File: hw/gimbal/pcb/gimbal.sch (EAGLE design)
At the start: 80 parts, among them J1 JST-XH4SMT_RA, T12 TPPAD1-13, T3 TPPAD1-13, T8 TPPAD1-13, U1 STM32F4R_64PIN, U2 TPS62172PWSON8, U3 TPS55330PQFN16, U4 MC33926, U5 DRV8313, U6 DRV8313, U7 AS5048A

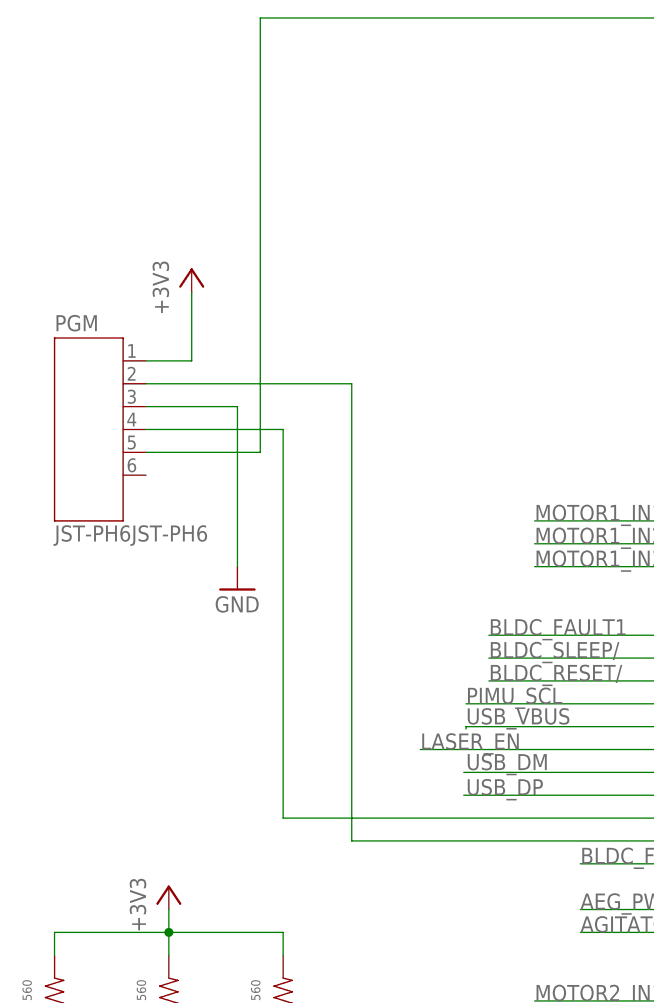
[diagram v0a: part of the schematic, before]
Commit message: gimbal: PCB: Fix the pin ordering on the programming connector.
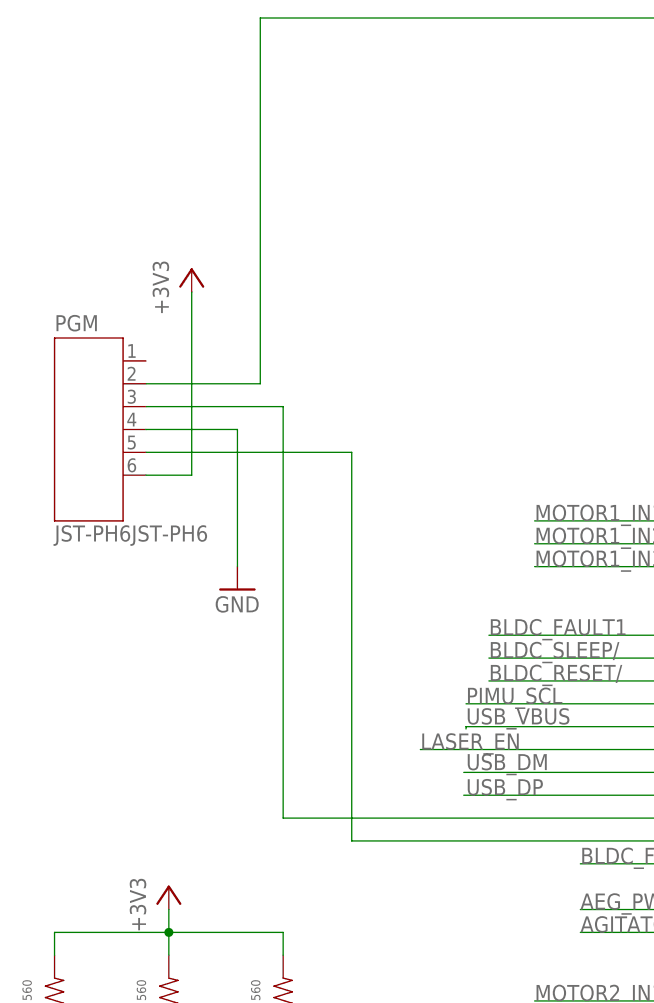
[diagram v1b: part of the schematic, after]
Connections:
- net +3V3: now also PGM.6; no longer PGM.1
- net GND: now also PGM.4; no longer PGM.3
- net N$24: now also PGM.2; no longer PGM.5
- net N$31: now also PGM.5; no longer PGM.2
- net N$32: now also PGM.3; no longer PGM.4
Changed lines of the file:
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@@
 </segment>
 <segment>
-<pinref part="PGM" gate="G$1" pin="3"/>
 <pinref part="GND16" gate="1" pin="GND"/>
-<wire x1="-30.48" y1="238.76" x2="-20.32" y2="238.76" width="0.1524" layer="91"/>
-<wire x1="-20.32" y1="238.76" x2="-20.32" y2="220.98" width="0.1524" layer="91"/>
+<pinref part="PGM" gate="G$1" pin="4"/>
+<wire x1="-20.32" y1="236.22" x2="-20.32" y2="220.98" width="0.1524" layer="91"/>
+<wire x1="-30.48" y1="236.22" x2="-20.32" y2="236.22" width="0.1524" layer="91"/>
 </segment>
 <segment>
@@
 </segment>
 <segment>
-<pinref part="PGM" gate="G$1" pin="1"/>
 <pinref part="+3V9" gate="G$1" pin="+3V3"/>
-<wire x1="-30.48" y1="243.84" x2="-25.4" y2="243.84" width="0.1524" layer="91"/>
-<wire x1="-25.4" y1="243.84" x2="-25.4" y2="251.46" width="0.1524" layer="91"/>
+<wire x1="-25.4" y1="251.46" x2="-25.4" y2="231.14" width="0.1524" layer="91"/>
+<pinref part="PGM" gate="G$1" pin="6"/>
+<wire x1="-25.4" y1="231.14" x2="-30.48" y2="231.14" width="0.1524" layer="91"/>
 </segment>
 <segment>
@@
 <junction x="101.6" y="264.16"/>
 <wire x1="101.6" y1="281.94" x2="-17.78" y2="281.94" width="0.1524" layer="91"/>
-<wire x1="-17.78" y1="281.94" x2="-17.78" y2="233.68" width="0.1524" layer="91"/>
-<pinref part="PGM" gate="G$1" pin="5"/>
-<wire x1="-17.78" y1="233.68" x2="-30.48" y2="233.68" width="0.1524" layer="91"/>
+<wire x1="-17.78" y1="281.94" x2="-17.78" y2="241.3" width="0.1524" layer="91"/>
 <pinref part="C6" gate="G$1" pin="P$1"/>
 <junction x="83.82" y="261.62"/>
+<pinref part="PGM" gate="G$1" pin="2"/>
+<wire x1="-17.78" y1="241.3" x2="-30.48" y2="241.3" width="0.1524" layer="91"/>
 </segment>
 </net>
 <net name="N$31" class="0">
 <segment>
-<pinref part="PGM" gate="G$1" pin="2"/>
-<wire x1="-30.48" y1="241.3" x2="-7.62" y2="241.3" width="0.1524" layer="91"/>
-<wire x1="-7.62" y1="241.3" x2="-7.62" y2="190.5" width="0.1524" layer="91"/>
 <pinref part="U1" gate="G$1" pin="PA14/SWCLK"/>
+<wire x1="-7.62" y1="233.68" x2="-7.62" y2="190.5" width="0.1524" layer="91"/>
 <wire x1="-7.62" y1="190.5" x2="48.006" y2="190.5" width="0.1524" layer="91"/>
+<pinref part="PGM" gate="G$1" pin="5"/>
+<wire x1="-30.48" y1="233.68" x2="-7.62" y2="233.68" width="0.1524" layer="91"/>
 </segment>
 </net>
 <net name="N$32" class="0">
 <segment>
-<wire x1="-15.24" y1="193.04" x2="-15.24" y2="236.22" width="0.1524" layer="91"/>
-<pinref part="PGM" gate="G$1" pin="4"/>
-<wire x1="-15.24" y1="236.22" x2="-30.48" y2="236.22" width="0.1524" layer="91"/>
+<wire x1="-15.24" y1="193.04" x2="-15.24" y2="238.76" width="0.1524" layer="91"/>
 <pinref part="U1" gate="G$1" pin="PA13/SWDIO"/>
 <wire x1="-15.24" y1="193.04" x2="48.006" y2="193.04" width="0.1524" layer="91"/>
-</segment>
-</net>
+<pinref part="PGM" gate="G$1" pin="3"/>
+<wire x1="-15.24" y1="238.76" x2="-30.48" y2="238.76" width="0.1524" layer="91"/>
+</segment>
+</net>

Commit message: gimbal: Start work on updating gimbal board to support mounting a joule shield on top of it.
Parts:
- removed C15: 100uF, mfpassives:CAPACITOR_P_6.3MM
- removed R19, R20: 1.69k, mfpassives:RESISTOR_0603
- removed SIMU: JST-ZH4, gimbal:JST-ZH4
- removed USB: MICRO-USB, gimbal:MICRO-USB
- removed USBI: (no value), gimbal:JST-PH4RA
- removed USBO: (no value), gimbal:JST-PH4SMT_VERT
- added C28, C29: 47uF, rcl:C-USC1206
- added J3: JST-XH4SMT_RA, gimbal:JST-XH4SMT_RA
- added J4: MF-CON-MICROUSB-RIGHT, mf_connectors:USB_MICRO_RIGHT
- added U$52, U$53, U$54, U$55: M2.5MOUNT, joule_shield:M2.5MOUNT
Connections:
- removed net N$12: USBI.1, USBO.1
- removed net N$13: USBI.2, USBO.2
- removed net N$14: USBI.3, USBO.3
- removed net N$15: USBI.4, USBO.4
- net +12V: now also C28.1, C29.1; no longer C15.P$1
- net +3V3: no longer R19.P$2, R20.P$2, SIMU.1
- net +8V: now also J3.4
- net GND: now also C28.2, C29.2, J3.1, J4.GND, J4.SLD; no longer C15.P$2, SIMU.4, USBG$1.5
- net SIMU_SCL: no longer R20.P$1, SIMU.3
- net SIMU_SDA: no longer R19.P$1, SIMU.2
- net SLAVE_RX: now also J3.3
- net SLAVE_TX: now also J3.2
- net USB_DM: now also J4.D-; no longer USBG$1.2
- net USB_DP: now also J4.D+; no longer USBG$1.3
- net USB_VBUS: now also J4.5V; no longer USBG$1.1

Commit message: WIP on 18V rs485 version of gimbal board
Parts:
- removed C28, C29: 47uF, rcl:C-USC1206
- removed C7: 4.7uF, mfpassives:CAPACITOR_NP_0603
- removed D4: DIODEB520C, gimbal:DIODEB520C
- removed J4: MF-CON-MICROUSB-RIGHT, mf_connectors:USB_MICRO_RIGHT
- removed L1: 2.2uH, gimbal:INDL1212
- removed PGM: JST-PH6JST-PH6, gimbal:JST-PH6JST-PH6
- removed R10, R8: 10k, mfpassives:RESISTOR_0603
- removed R11: 78.7k, mfpassives:RESISTOR_0603
- removed R12: 1.87k, mfpassives:RESISTOR_0603
- removed R14: 220, mfpassives:RESISTOR_0603
- removed R9: 88.7k, mfpassives:RESISTOR_0603
- removed T12, T3, T8, TG: TPPAD1-13, testpad:TPPAD1-13
- removed U$52, U$53, U$54, U$55: M2.5MOUNT, joule_shield:M2.5MOUNT
- added C15: 0.1uF 50V, mfpassives:CAPACITOR_NP_0402
- added SWD: JST-ZH6SMT_VERT, controller:JST-ZH6SMT_VERT
- ARM: AMFPN JS102011SAQN -> (none); DPN 401-1999-1-ND -> (none); MPN (none) -> JS102011SAQN; POPULATE (none) -> 1
- C1: value 4.7uF -> 10uF 35V; device mfpassives:CAPACITOR_NP_0603 -> mfpassives:CAPACITOR_NP_1206; AMFPN CC0603KRX5R6BB475 -> (none); DPN 311-1455-1-ND -> (none); MF (none) -> TDK; MPN (none) -> CGA5L1X7R1V106K160AC
- C10: value 10uF -> 0.1uF 50V; device mfpassives:CAPACITOR_NP_1206 -> mfpassives:CAPACITOR_NP_0402; AMFPN MF-CAP-1206-10uF -> (none); MF (none) -> Walsin; MPN (none) -> 0402B104K500CT
- C11, C17, C18, C19: value 22uF 16V -> 10uF 35V; device mfpassives:CAPACITOR_NP_1210 -> mfpassives:CAPACITOR_NP_1206; AMFPN C3225X7R1C226M250AC -> (none); DPN 445-3955-1-ND -> (none); MF (none) -> TDK; MPN (none) -> CGA5L1X7R1V106K160AC
- C12, C16: value 10uF -> 10uF 35V; AMFPN MF-CAP-1206-10uF -> (none); MF (none) -> TDK; MPN (none) -> CGA5L1X7R1V106K160AC
- C13: value 0.047uF -> 10uF 35V; device mfpassives:CAPACITOR_NP_0603 -> mfpassives:CAPACITOR_NP_1206; AMFPN GRM188R71E473KA01D -> (none); DPN 490-1522-1-ND -> (none); MF (none) -> TDK; MPN (none) -> CGA5L1X7R1V106K160AC
- C14: value 0.1uF -> 10uF 35V; device mfpassives:CAPACITOR_NP_0603 -> mfpassives:CAPACITOR_NP_1206; AMFPN MF-CAP-0603-0.1uF -> (none); MF (none) -> TDK; MPN (none) -> CGA5L1X7R1V106K160AC
- C2, C20, C21, C22, C24, C26, C27, C3, C4, C5, C6: value 0.1uF -> 0.1uF 50V; device mfpassives:CAPACITOR_NP_0603 -> mfpassives:CAPACITOR_NP_0402; AMFPN MF-CAP-0603-0.1uF -> (none); MF (none) -> Walsin; MPN (none) -> 0402B104K500CT
- C23, C25: AMFPN MF-CAP-0603-0.01uF -> (none); HOUSEPART (none) -> YES; MPN (none) -> MF-CAP-0603-0.01uF
- C8, C9: AMFPN MF-CAP-0603-10pF -> (none); HOUSEPART (none) -> YES; MPN (none) -> MF-CAP-0603-10pF
- D1: device mfleds:LED_SINGLE_0603 -> mfleds:LED_SINGLE-0603-RED; AMFPN MF-LED-0603-GREEN -> (none)
- D2, D3: device mfleds:LED_SINGLE_0603 -> mfleds:LED_SINGLE-0603-RED; AMFPN MF-LED-0603-RED -> (none)
- J1, J3: AMFPN S4B-XH-SM4-TB(LF)(SN) -> (none); DPN 455-2262-1-ND -> (none); MF (none) -> JST; MPN (none) -> S4B-XH-SM4-TB(LF)(SN); POPULATE (none) -> 1
- J2, M1, M2, MOUNT1, MOUNT2: POPULATE (none) -> 0
- L2: value 2.2uH -> 10uH; device gimbal:INDASPI-6045S -> mfpassives:INDUCTOR_1210; AMFPN ASPI-6045S-2R2N-T -> (none); DPN ASPI-6045S-2R2N-TCT-ND -> (none); HOUSEPART (none) -> 1; MPN (none) -> MF-IND-1210-10uH; POPULATE (none) -> 1
- PABS, PI: AMFPN B4B-ZR-SM4-TF(LF)(SN) -> (none); DPN 455-1683-1-ND -> (none); MF (none) -> JST; MPN (none) -> B4B-ZR-SM4-TF(LF)(SN); POPULATE (none) -> 1
- Q1: AMFPN ABM3B-8.000MHZ-10-1-U-T -> (none); DPN 535-9721-1-ND -> (none); MPN (none) -> ABM3B-8.000MHZ-10-1-U-T; POPULATE (none) -> 1
- R1: value 10 -> 560; AMFPN MF-RES-0603-10 -> (none); HOUSEPART (none) -> YES; MPN (none) -> MF-RES-0603-560
- R13, R5: value 100k -> 18k; AMFPN ERJ-3EKF1003V -> (none); DPN P100KHCT-ND -> (none); HOUSEPART (none) -> YES; MPN (none) -> MF-RES-0603-18K
- R15, R16, R17, R18: AMFPN MF-RES-0603-1.69K -> (none); HOUSEPART (none) -> YES; MPN (none) -> MF-RES-0603-1.69K
- R2, R3, R4: AMFPN MF-RES-0603-560 -> (none); HOUSEPART (none) -> YES; MPN (none) -> MF-RES-0603-560
- R6: value 10k -> 1.69k; AMFPN ERJ-3EKF1002V -> (none); DPN P10.0KHCT-ND -> (none); HOUSEPART (none) -> YES; MPN (none) -> MF-RES-0603-1.69K
- R7: value 100k -> 560; AMFPN ERJ-3EKF1003V -> (none); DPN P100KHCT-ND -> (none); HOUSEPART (none) -> YES; MPN (none) -> MF-RES-0603-560
- U1: AMFPN STM32F411RET6 -> (none); DPN 497-14909-ND -> (none); MF (none) -> ST; MPN (none) -> STM32F411RET6; POPULATE (none) -> 1
- U2: value TPS62172PWSON8 -> MAX13431E; device gimbal:TPS62172PWSON8 -> controller:MAX13431E; AMFPN TPS62172DSGT -> (none); DPN 296-29879-1-ND -> (none); MF (none) -> Maxim; MPN (none) -> MAX13431EETB+T; POPULATE (none) -> 1
- U3: value TPS55330PQFN16 -> TPS62177WSON10; device gimbal:TPS55330PQFN16 -> imu_junction:TPS62177WSON10; AMFPN TPS55330RTET -> (none); DPN 296-36219-1-ND -> (none); MF (none) -> TI; MPN (none) -> TPS62177DQCR; POPULATE (none) -> 1
- U4: AMFPN MC33926PNBR2 -> (none); DPN MC33926PNBR2CT-ND -> (none); MF (none) -> Freescale; MPN (none) -> MC33926PNBR2; POPULATE (none) -> 1
- U5, U6: AMFPN DRV8313PWP -> (none); DPN 296-35540-5-ND -> (none); MF (none) -> TI; MPN (none) -> DRV8313PWP; POPULATE (none) -> 1
- U7: AMFPN AS5048A-HTSP-500 -> (none); DPN AS5048A-HTSP-500CT-ND -> (none); MF (none) -> austriamicrosystems; MPN (none) -> AS5048A-HTSP-500; POPULATE (none) -> 1
- U8: AMFPN MF-DSC-SOT233-BSS138 -> (none); HOUSEPART (none) -> YES; MPN (none) -> MF-DSC-SOT233-BSS138; POPULATE (none) -> 1
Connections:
- removed net +12V: C16.P$1, C22.P$1, C24.P$1, C28.1, C29.1, D4.1, R7.P$2, R9.P$2, T12.TP, U5.VM1, U5.VM2, U6.VM1, U6.VM2
- removed net BOOST_EN: U1.PC3/SPI2_MOSI, U3.EN
- removed net N$16: L1.P$1, U2.SW
- removed net N$17: D4.2, L2.P$2, U3.SW1, U3.SW2, U3.SW3
- removed net N$18: R11.P$2, U3.FREQ
- removed net N$19: C14.P$1, R12.P$1
- removed net N$20: R12.P$2, U3.COMP
- removed net N$21: C13.P$1, U3.SS
- removed net N$22: R10.P$2, R9.P$1, U3.FB
- removed net N$38: R7.P$1, R8.P$2, U1.PC2/SPI2_MISO
- removed net SIMU_SCL: U1.PB10/TIM2_3/I2C2_SCL/SPI2_SCK
- removed net SIMU_SDA: U1.PB9/TIM4_4/TIM11_1/I2C1_SDA/I2C2_SDA
- removed net USB_DM: J4.D-, U1.PA11/TIM1_4/SPI4_MISO/UART6_TX/USB_DM
- removed net USB_DP: J4.D+, U1.PA12/SPI5_MISO/UART6_RX/USB_DP
- removed net USB_VBUS: J4.5V, U1.PA9/TIM1_2/UART1_TX/USB_VBUS
- new net D1_N: J1.3, J3.3, U2.B
- new net D1_P: J1.2, J3.2, U2.A
- new net DIR3: U2.DE, U2.RE/
- new net N$4: L2.P$1, U3.SW
- net +3V3: now also C10.P$1, C13.P$1, C14.P$1, C15.P$1, L2.P$2, SWD.6, U2.VCC, U2.VL, U3.SLEEP, U3.VOS; no longer C1.P$1, C11.P$1, L1.P$2, PGM.6, T3.TP, U2.VOS
- net +8V: now also C11.P$1, C16.P$1, C22.P$1, C24.P$1, U3.EN, U5.VM1, U5.VM2, U6.VM1, U6.VM2; no longer C10.P$1, L2.P$1, T8.TP, U2.EN, U2.VIN
- net GND: now also C15.P$2, R7.P$1, SWD.4, U2.GND, U3.FB, U3.NC, U3.PGND; no longer C28.2, C29.2, C7.P$2, J4.GND, J4.SLD, PGM.4, R10.P$1, R11.P$1, R14.P$1, R8.P$1, TG.TP, U2.AGND, U2.FB, U2.PGND, U3.PGND1, U3.PGND2, U3.PGND3
- net MOTOR_FB: now also R7.P$2; no longer R14.P$2
- net N$23: now also C1.P$1; no longer C7.P$1
- net N$24: now also SWD.2; no longer PGM.2
- net N$31: now also SWD.5; no longer PGM.5
- net N$32: now also SWD.3; no longer PGM.3
- net SLAVE_RX: now also U2.RO; no longer J1.3, J3.3
- net SLAVE_TX: now also U2.DI; no longer J1.2, J3.2
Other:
- moved on the sheet: J3, R1, R13, R15, R16, R17, R18, R2, R3, R4, R5, R6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

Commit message: More work on gimbal v4
Power and ground now largely routed
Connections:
- net +8V renamed +18V
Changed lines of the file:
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@@
 <part name="+3V6" library="supply1" deviceset="+3V3" device=""/>
 <part name="GND11" library="supply1" deviceset="GND" device=""/>
-<part name="SUPPLY3" library="supply2" deviceset="+8V" device=""/>
+<part name="SUPPLY3" library="supply2" deviceset="+18V" device=""/>
 <part name="GND12" library="supply1" deviceset="GND" device=""/>
 <part name="GND13" library="supply1" deviceset="GND" device=""/>
@@
 </part>
 <part name="GND17" library="supply1" deviceset="GND" device=""/>
-<part name="SUPPLY4" library="supply2" deviceset="+8V" device=""/>
+<part name="SUPPLY4" library="supply2" deviceset="+18V" device=""/>
 <part name="GND18" library="supply1" deviceset="GND" device=""/>
 <part name="ARM" library="gimbal" deviceset="SLIDE_SWITCH" device="JS_SUB_SWITCH">
@@
 <attribute name="MPN" value="CGA5L1X7R1V106K160AC"/>
 </part>
-<part name="SUPPLY5" library="supply2" deviceset="+8V" device=""/>
+<part name="SUPPLY5" library="supply2" deviceset="+18V" device=""/>
 <part name="R17" library="mfpassives" deviceset="RESISTOR" device="_0603" value="1.69k">
 <attribute name="HOUSEPART" value="YES"/>
@@
 <attribute name="POPULATE" value="1"/>
 </part>
-<part name="SUPPLY2" library="supply2" deviceset="+8V" device=""/>
-<part name="SUPPLY6" library="supply2" deviceset="+8V" device=""/>
+<part name="SUPPLY2" library="supply2" deviceset="+18V" device=""/>
+<part name="SUPPLY6" library="supply2" deviceset="+18V" device=""/>
 <part name="U3" library="imu_junction" deviceset="TPS62177" device="WSON10">
 <attribute name="MF" value="TI"/>
@@
 <attribute name="MPN" value="0402B104K500CT"/>
 </part>
-<part name="SUPPLY7" library="supply2" deviceset="+8V" device=""/>
+<part name="SUPPLY7" library="supply2" deviceset="+18V" device=""/>
 <part name="GND7" library="supply1" deviceset="GND" device=""/>
 <part name="U2" library="controller" deviceset="MAX13431E" device="">
@@
 <instance part="+3V6" gate="G$1" x="25.4" y="-292.1"/>
 <instance part="GND11" gate="1" x="101.6" y="-403.86"/>
-<instance part="SUPPLY3" gate="+8V" x="111.76" y="-375.92"/>
+<instance part="SUPPLY3" gate="+18V" x="111.76" y="-375.92"/>
 <instance part="GND12" gate="1" x="63.5" y="-210.82"/>
 <instance part="GND13" gate="1" x="226.06" y="-210.82"/>
@@
 </instance>
 <instance part="GND17" gate="1" x="203.2" y="142.24"/>
-<instance part="SUPPLY4" gate="+8V" x="226.06" y="236.22"/>
+<instance part="SUPPLY4" gate="+18V" x="226.06" y="236.22"/>
 <instance part="GND18" gate="1" x="226.06" y="180.34"/>
 <instance part="ARM" gate="G$1" x="104.14" y="-101.6">
@@
 <attribute name="MF" x="60.96" y="-48.26" size="1.778" layer="96" display="off"/>
 </instance>
-<instance part="SUPPLY5" gate="+8V" x="43.18" y="-17.78"/>
+<instance part="SUPPLY5" gate="+18V" x="43.18" y="-17.78"/>
 <instance part="R17" gate="G$1" x="91.44" y="-314.96" rot="R180"/>
 <instance part="R18" gate="G$1" x="96.52" y="-314.96" rot="R180"/>
@@
 <attribute name="POPULATE" x="48.26" y="-388.62" size="1.778" layer="96" display="off"/>
 </instance>
-<instance part="SUPPLY2" gate="+8V" x="7.62" y="-121.92"/>
-<instance part="SUPPLY6" gate="+8V" x="167.64" y="-127"/>
+<instance part="SUPPLY2" gate="+18V" x="7.62" y="-121.92"/>
+<instance part="SUPPLY6" gate="+18V" x="167.64" y="-127"/>
 <instance part="U3" gate="G$1" x="170.18" y="58.42">
 <attribute name="MPN" x="170.18" y="58.42" size="1.778" layer="96" display="off"/>
@@
 <attribute name="MF" x="226.06" y="53.34" size="1.778" layer="96" display="off"/>
 </instance>
-<instance part="SUPPLY7" gate="+8V" x="132.08" y="76.2"/>
+<instance part="SUPPLY7" gate="+18V" x="132.08" y="76.2"/>
 <instance part="GND7" gate="1" x="111.76" y="-469.9"/>
 <instance part="U2" gate="G$1" x="78.74" y="-444.5">
@@
 </segment>
 </net>
-<net name="+8V" class="0">
+<net name="+18V" class="0">
 <segment>
 <pinref part="J1" gate="G$1" pin="4"/>
-<pinref part="SUPPLY3" gate="+8V" pin="+8V"/>
+<pinref part="SUPPLY3" gate="+18V" pin="+18V"/>
 <wire x1="88.9" y1="-391.16" x2="111.76" y2="-391.16" width="0.1524" layer="91"/>
 <wire x1="111.76" y1="-391.16" x2="111.76" y2="-378.46" width="0.1524" layer="91"/>
@@
 </segment>
 <segment>
-<pinref part="SUPPLY4" gate="+8V" pin="+8V"/>
+<pinref part="SUPPLY4" gate="+18V" pin="+18V"/>
 <wire x1="226.06" y1="233.68" x2="226.06" y2="231.14" width="0.1524" layer="91"/>
 <pinref part="R5" gate="G$1" pin="P$2"/>
@@
 <pinref part="C18" gate="G$1" pin="P$1"/>
 <pinref part="C19" gate="G$1" pin="P$1"/>
-<pinref part="SUPPLY5" gate="+8V" pin="+8V"/>
+<pinref part="SUPPLY5" gate="+18V" pin="+18V"/>
 <junction x="43.18" y="-20.32"/>
 </segment>
@@
 <wire x1="12.7" y1="-137.16" x2="17.78" y2="-137.16" width="0.1524" layer="91"/>
 <pinref part="C22" gate="G$1" pin="P$1"/>
-<pinref part="SUPPLY2" gate="+8V" pin="+8V"/>
+<pinref part="SUPPLY2" gate="+18V" pin="+18V"/>
 <pinref part="C11" gate="G$1" pin="P$1"/>
 <wire x1="7.62" y1="-124.46" x2="-27.94" y2="-124.46" width="0.1524" layer="91"/>
@@
 <wire x1="170.18" y1="-139.7" x2="177.8" y2="-139.7" width="0.1524" layer="91"/>
 <pinref part="C24" gate="G$1" pin="P$1"/>
-<pinref part="SUPPLY6" gate="+8V" pin="+8V"/>
+<pinref part="SUPPLY6" gate="+18V" pin="+18V"/>
 <pinref part="C16" gate="G$1" pin="P$1"/>
 <wire x1="132.08" y1="-137.16" x2="132.08" y2="-132.08" width="0.1524" layer="91"/>
@@
 <wire x1="132.08" y1="68.58" x2="132.08" y2="53.34" width="0.1524" layer="91"/>
 <junction x="132.08" y="68.58"/>
-<pinref part="SUPPLY7" gate="+8V" pin="+8V"/>
-</segment>
-</net>
+<pinref part="SUPPLY7" gate="+18V" pin="+18V"/>
+</segment>
+</net>

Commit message: More work on gimbal r4
I think everything is ready now
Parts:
- removed J3: JST-XH4SMT_RA, gimbal:JST-XH4SMT_RA
- added JW: (no value), pinhead:PINHD-2X4
- J2: value (none) -> JST-XH4SMT_RA; device pinhead:PINHD-2X4 -> gimbal:JST-XH4SMT_RA; MF (none) -> JST; MPN (none) -> S4B-XH-SM4-TB(LF)(SN); POPULATE 0 -> 1
- U7: MF austriamicrosystems -> AMS; MPN AS5048A-HTSP-500 -> AS5047P-ATSM
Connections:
- removed net DIR3: U2.DE, U2.RE/
- new net SLAVE_DIR: U1.PC8/TIM3_3, U2.DE, U2.RE/
- net +18V: now also J2.4; no longer J3.4
- net +3V3: now also JW.5; no longer J2.5
- net D1_N: now also J2.3; no longer J3.3
- net D1_P: now also J2.2; no longer J3.2
- net GND: now also J2.1, JW.2, JW.4; no longer J2.2, J2.4, J3.1
- net N$1: now also JW.6; no longer J2.6
- net N$2: now also JW.3; no longer J2.3
- net N$3: now also JW.1; no longer J2.1
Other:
- moved on the sheet: C6, R1

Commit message: gimbal: Replace 10uF cap with one that exists
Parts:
- C1, C11, C12, C13, C14, C16, C17, C18, C19: MPN CGA5L1X7R1V106K160AC -> CGA5L1X7R1V106M160AE
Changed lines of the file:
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@@
 <part name="C17" library="mfpassives" deviceset="CAPACITOR_NP" device="_1206" value="10uF 35V">
 <attribute name="MF" value="TDK"/>
-<attribute name="MPN" value="CGA5L1X7R1V106K160AC"/>
+<attribute name="MPN" value="CGA5L1X7R1V106M160AE"/>
 </part>
 <part name="C18" library="mfpassives" deviceset="CAPACITOR_NP" device="_1206" value="10uF 35V">
 <attribute name="MF" value="TDK"/>
-<attribute name="MPN" value="CGA5L1X7R1V106K160AC"/>
+<attribute name="MPN" value="CGA5L1X7R1V106M160AE"/>
 </part>
 <part name="C19" library="mfpassives" deviceset="CAPACITOR_NP" device="_1206" value="10uF 35V">
 <attribute name="MF" value="TDK"/>
-<attribute name="MPN" value="CGA5L1X7R1V106K160AC"/>
+<attribute name="MPN" value="CGA5L1X7R1V106M160AE"/>
 </part>
 <part name="SUPPLY5" library="supply2" deviceset="+18V" device=""/>
@@
 <part name="C13" library="mfpassives" deviceset="CAPACITOR_NP" device="_1206" value="10uF 35V">
 <attribute name="MF" value="TDK"/>
-<attribute name="MPN" value="CGA5L1X7R1V106K160AC"/>
+<attribute name="MPN" value="CGA5L1X7R1V106M160AE"/>
 </part>
 <part name="C14" library="mfpassives" deviceset="CAPACITOR_NP" device="_1206" value="10uF 35V">
 <attribute name="MF" value="TDK"/>
-<attribute name="MPN" value="CGA5L1X7R1V106K160AC"/>
+<attribute name="MPN" value="CGA5L1X7R1V106M160AE"/>
 </part>
 <part name="C12" library="mfpassives" deviceset="CAPACITOR_NP" device="_1206" value="10uF 35V">
 <attribute name="MF" value="TDK"/>
-<attribute name="MPN" value="CGA5L1X7R1V106K160AC"/>
+<attribute name="MPN" value="CGA5L1X7R1V106M160AE"/>
 </part>
 <part name="C15" library="mfpassives" deviceset="CAPACITOR_NP" device="_0402" value="0.1uF 50V">
@@
 <part name="C11" library="mfpassives" deviceset="CAPACITOR_NP" device="_1206" value="10uF 35V">
 <attribute name="MF" value="TDK"/>
-<attribute name="MPN" value="CGA5L1X7R1V106K160AC"/>
+<attribute name="MPN" value="CGA5L1X7R1V106M160AE"/>
 </part>
 <part name="C16" library="mfpassives" deviceset="CAPACITOR_NP" device="_1206" value="10uF 35V">
 <attribute name="MF" value="TDK"/>
-<attribute name="MPN" value="CGA5L1X7R1V106K160AC"/>
+<attribute name="MPN" value="CGA5L1X7R1V106M160AE"/>
 </part>
 <part name="GND3" library="supply1" deviceset="GND" device=""/>
@@
 <part name="C1" library="mfpassives" deviceset="CAPACITOR_NP" device="_1206" value="10uF 35V">
 <attribute name="MF" value="TDK"/>
-<attribute name="MPN" value="CGA5L1X7R1V106K160AC"/>
+<attribute name="MPN" value="CGA5L1X7R1V106M160AE"/>
 </part>
 </parts>
